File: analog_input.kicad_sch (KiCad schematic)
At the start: 36 parts, among them J2 5 Pin 3.5mm, Q1 MMBT2222A 1P, U4 LM358, U5 LM358

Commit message: routed version
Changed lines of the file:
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@@
   (junction (at 81.28 132.08) (diameter 0) (color 0 0 0 0)
-  )
-  (junction (at 212.09 67.31) (diameter 0) (color 0 0 0 0)
   )
   (junction (at 128.27 129.54) (diameter 0) (color 0 0 0 0)
@@
     (stroke (width 0) (type default))
   )
-  (wire (pts (xy 241.3 133.35) (xy 245.11 133.35))
+  (wire (pts (xy 240.03 133.35) (xy 245.11 133.35))
     (stroke (width 0) (type default))
   )
@@
     (stroke (width 0) (type default))
   )
-  (wire (pts (xy 212.09 62.23) (xy 212.09 67.31))
+  (wire (pts (xy 210.82 64.77) (xy 210.82 67.31))
     (stroke (width 0) (type default))
   )
@@
     (stroke (width 0) (type default))
   )
-  (wire (pts (xy 210.82 67.31) (xy 212.09 67.31))
-    (stroke (width 0) (type default))
-  )
   (wire (pts (xy 199.39 57.15) (xy 220.98 57.15))
     (stroke (width 0) (type default))
@@
     (stroke (width 0) (type default))
   )
+  (wire (pts (xy 260.35 22.86) (xy 259.08 22.86))
+    (stroke (width 0) (type default))
+  )
   (wire (pts (xy 49.53 92.71) (xy 54.61 92.71))
     (stroke (width 0) (type default))
@@
     (stroke (width 0) (type default))
   )
-  (wire (pts (xy 212.09 67.31) (xy 213.36 67.31))
-    (stroke (width 0) (type default))
-  )
   (wire (pts (xy 87.63 74.93) (xy 83.82 74.93))
     (stroke (width 0) (type default))
@@
   )
   (wire (pts (xy 191.77 57.15) (xy 187.96 57.15))
+    (stroke (width 0) (type default))
+  )
+  (wire (pts (xy 260.35 33.02) (xy 259.08 33.02))
     (stroke (width 0) (type default))
   )
@@
     )
   )
+  (netclass_flag "" (length 2.54) (shape round) (at 238.76 72.39 0) (fields_autoplaced)
+    (effects (font (size 1.27 1.27)) (justify left bottom))
+    (property "Netclass" "Power" (at 239.3696 69.85 0)
+      (effects (font (size 1.27 1.27) italic) (justify left))
+    )
+  )
   (symbol (lib_id "Device:R") (at 62.23 87.63 90) (unit 1)
     (in_bom yes) (on_board yes) (dnp no) (fields_autoplaced)
@@
     )
   )
-  (symbol (lib_id "power:VAA") (at 212.09 62.23 0) (unit 1)
-    (in_bom yes) (on_board yes) (dnp no) (fields_autoplaced)
-    (property "Reference" "#PWR0156" (at 212.09 66.04 0)
-      (effects (font (size 1.27 1.27)) hide)
-    )
-    (property "Value" "VAA" (at 214.63 60.9599 0)
-      (effects (font (size 1.27 1.27)) (justify left))
-    )
-    (property "Footprint" "" (at 212.09 62.23 0)
-      (effects (font (size 1.27 1.27)) hide)
-    )
-    (property "Datasheet" "" (at 212.09 62.23 0)
+  (symbol (lib_id "power:VAA") (at 210.82 64.77 0) (unit 1)
+    (in_bom yes) (on_board yes) (dnp no) (fields_autoplaced)
+    (property "Reference" "#PWR0156" (at 210.82 68.58 0)
+      (effects (font (size 1.27 1.27)) hide)
+    )
+    (property "Value" "VAA" (at 213.36 63.4999 0)
+      (effects (font (size 1.27 1.27)) (justify left))
+    )
+    (property "Footprint" "" (at 210.82 64.77 0)
+      (effects (font (size 1.27 1.27)) hide)
+    )
+    (property "Datasheet" "" (at 210.82 64.77 0)
       (effects (font (size 1.27 1.27)) hide)
     )
@@
     )
   )
-  (symbol (lib_id "power:VAA") (at 241.3 133.35 90) (unit 1)
-    (in_bom yes) (on_board yes) (dnp no) (fields_autoplaced)
-    (property "Reference" "#PWR071" (at 245.11 133.35 0)
-      (effects (font (size 1.27 1.27)) hide)
-    )
-    (property "Value" "VAA" (at 237.49 133.3499 90)
-      (effects (font (size 1.27 1.27)) (justify left))
-    )
-    (property "Footprint" "" (at 241.3 133.35 0)
-      (effects (font (size 1.27 1.27)) hide)
-    )
-    (property "Datasheet" "" (at 241.3 133.35 0)
+  (symbol (lib_id "power:VAA") (at 240.03 133.35 90) (unit 1)
+    (in_bom yes) (on_board yes) (dnp no) (fields_autoplaced)
+    (property "Reference" "#PWR071" (at 243.84 133.35 0)
+      (effects (font (size 1.27 1.27)) hide)
+    )
+    (property "Value" "VAA" (at 236.22 133.3499 90)
+      (effects (font (size 1.27 1.27)) (justify left))
+    )
+    (property "Footprint" "" (at 240.03 133.35 0)
+      (effects (font (size 1.27 1.27)) hide)
+    )
+    (property "Datasheet" "" (at 240.03 133.35 0)
       (effects (font (size 1.27 1.27)) hide)
     )
@@
       (effects (font (size 1.27 1.27)) hide)
     )
-    (property "Value" "GNDA" (at 127 104.14 0)
+    (property "Value" "GNDA" (at 127 102.87 0)
       (effects (font (size 1.27 1.27)))
     )
@@
       (effects (font (size 1.27 1.27)) hide)
     )
-    (property "Value" "GNDA" (at 128.27 143.51 0)
+    (property "Value" "GNDA" (at 128.27 142.24 0)
       (effects (font (size 1.27 1.27)))
     )
@@
     )
   )
-  (symbol (lib_id "power:+10V") (at 259.08 22.86 270) (unit 1)
-    (in_bom yes) (on_board yes) (dnp no) (fields_autoplaced)
-    (property "Reference" "#PWR048" (at 255.27 22.86 0)
-      (effects (font (size 1.27 1.27)) hide)
-    )
-    (property "Value" "+10V" (at 262.89 22.8599 90)
-      (effects (font (size 1.27 1.27)) (justify left))
-    )
-    (property "Footprint" "" (at 259.08 22.86 0)
-      (effects (font (size 1.27 1.27)) hide)
-    )
-    (property "Datasheet" "" (at 259.08 22.86 0)
+  (symbol (lib_id "power:+10V") (at 260.35 22.86 270) (unit 1)
+    (in_bom yes) (on_board yes) (dnp no) (fields_autoplaced)
+    (property "Reference" "#PWR048" (at 256.54 22.86 0)
+      (effects (font (size 1.27 1.27)) hide)
+    )
+    (property "Value" "+10V" (at 264.16 22.8599 90)
+      (effects (font (size 1.27 1.27)) (justify left))
+    )
+    (property "Footprint" "" (at 260.35 22.86 0)
+      (effects (font (size 1.27 1.27)) hide)
+    )
+    (property "Datasheet" "" (at 260.35 22.86 0)
       (effects (font (size 1.27 1.27)) hide)
     )
@@
     )
   )
-  (symbol (lib_id "power:GNDA") (at 259.08 33.02 90) (unit 1)
-    (in_bom yes) (on_board yes) (dnp no) (fields_autoplaced)
-    (property "Reference" "#PWR049" (at 265.43 33.02 0)
-      (effects (font (size 1.27 1.27)) hide)
-    )
-    (property "Value" "GNDA" (at 262.89 33.0199 90)
+  (symbol (lib_id "power:GNDA") (at 260.35 33.02 90) (unit 1)
+    (in_bom yes) (on_board yes) (dnp no) (fields_autoplaced)
+    (property "Reference" "#PWR049" (at 266.7 33.02 0)
+      (effects (font (size 1.27 1.27)) hide)
+    )
+    (property "Value" "GNDA" (at 264.16 33.0199 90)
       (effects (font (size 1.27 1.27)) (justify right))
     )
-    (property "Footprint" "" (at 259.08 33.02 0)
-      (effects (font (size 1.27 1.27)) hide)
-    )
-    (property "Datasheet" "" (at 259.08 33.02 0)
+    (property "Footprint" "" (at 260.35 33.02 0)
+      (effects (font (size 1.27 1.27)) hide)
+    )
+    (property "Datasheet" "" (at 260.35 33.02 0)
       (effects (font (size 1.27 1.27)) hide)
     )
@@
       (effects (font (size 1.27 1.27)) hide)
     )
-    (property "Value" "GNDA" (at 121.92 62.23 0)
-      (effects (font (size 1.27 1.27)))
-    )
+    (property "Value" "GNDA" (at 121.92 60.96 0)
+      (effects (font (size 1.27 1.27)))
+    )

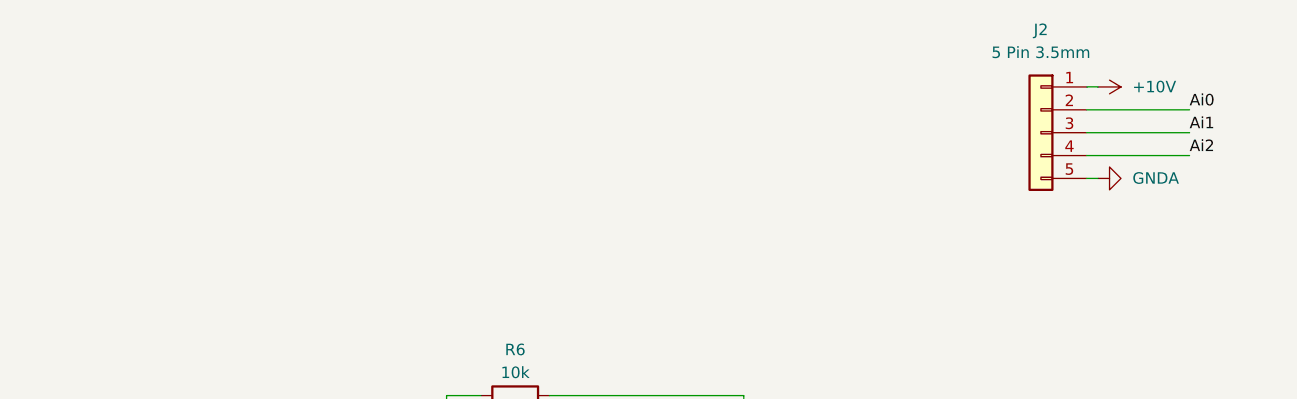
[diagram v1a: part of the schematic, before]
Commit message: Preparation for future use.
Reworked to use i2c bus expanders.
added sketch for add-on boards.
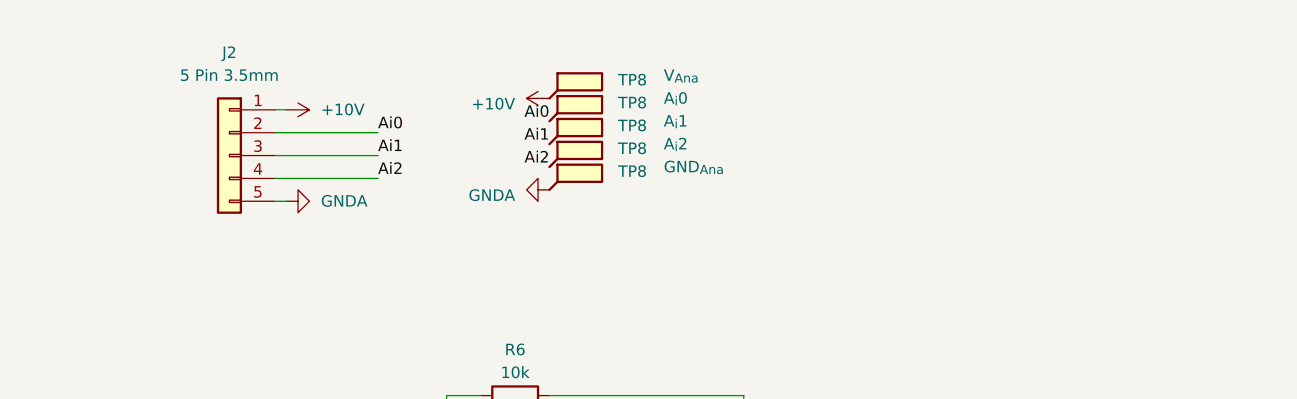
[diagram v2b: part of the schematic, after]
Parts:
- added TP8: V_{Ana}, TestPoint:TestPoint_Pad_1.0x1.0mm, symbol Connector:TestPoint_Flag
- added TP8: A_{i}2, TestPoint:TestPoint_Pad_1.0x1.0mm, symbol Connector:TestPoint_Flag
- added TP8: GND_{Ana}, TestPoint:TestPoint_Pad_1.0x1.0mm, symbol Connector:TestPoint_Flag
- added TP8: A_{i}1, TestPoint:TestPoint_Pad_1.0x1.0mm, symbol Connector:TestPoint_Flag
- added TP8: A_{i}0, TestPoint:TestPoint_Pad_1.0x1.0mm, symbol Connector:TestPoint_Flag
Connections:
- net +10V: now also TP8.1
- net Ai0: now also TP8.1
- net Ai1: now also TP8.1
- net Ai2: now also TP8.1
- net GNDA: now also TP8.1
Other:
- moved on the sheet: J2
